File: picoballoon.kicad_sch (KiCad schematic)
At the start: 31 parts, among them J1 SOLAR+, J2 SOLAR-, Q1 AO3401A, Q2 DTC143ZEBTL, U1 SPV1040, U2 STM32G070RBTx, U3 L70-R, U4 GPS1003

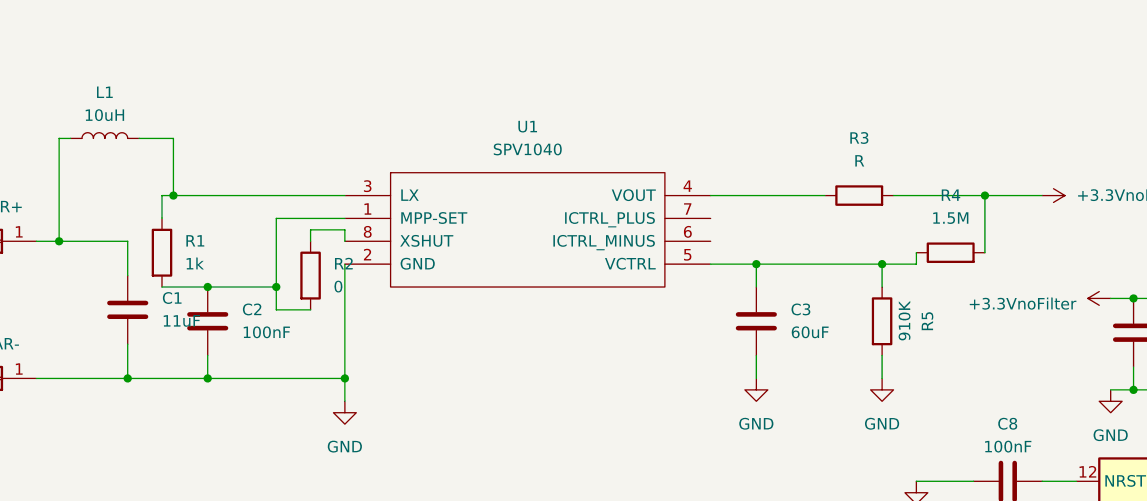
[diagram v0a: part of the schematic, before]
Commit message: Completed SPV1040 compoment wiring with new solar panel values.
Also calculated power draw from GPS and MCU in a spreadsheet. These will
be needed to calculate max power to charge supercap with.
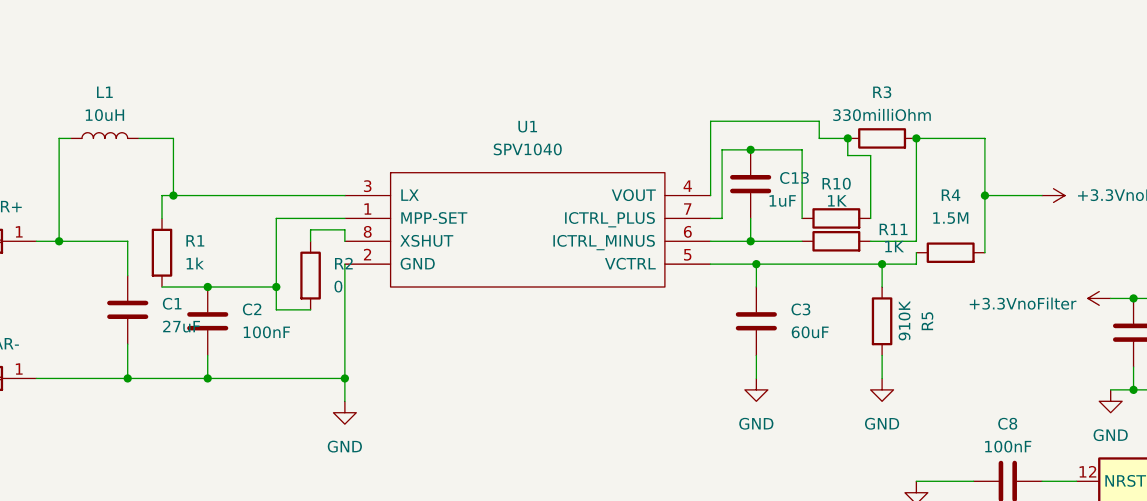
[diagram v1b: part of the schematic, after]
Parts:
- added C13: 1uF, symbol Device:C
- added R10, R11: 1K, symbol Device:R
- C1: value 11uF -> 27uF
- R3: value R -> 330milliOhm
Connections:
- net +3.3V: now also R11.2
- net at R3.1, U1.4 (VOUT): now also R10.2
- net at U1.6 (ICTRL_MINUS): now also C13.1, R11.1
- net at U1.7 (ICTRL_PLUS): now also C13.2, R10.1
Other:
- moved on the sheet: R3
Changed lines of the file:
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@@
   (junction (at 262.255 25.4) (diameter 0) (color 0 0 0 0)
   )
+  (junction (at 100.965 25.4) (diameter 0) (color 0 0 0 0)
+  )
   (junction (at 143.51 41.91) (diameter 0) (color 0 0 0 0)
   )
@@
   (junction (at 281.94 31.115) (diameter 0) (color 0 0 0 0)
   )
+  (junction (at 111.76 24.13) (diameter 0) (color 0 0 0 0)
+  )
+  (junction (at 100.965 35.56) (diameter 0) (color 0 0 0 0)
+  )
   (junction (at 219.075 32.385) (diameter 0) (color 0 0 0 0)
   )
@@
   (junction (at 269.24 57.785) (diameter 0) (color 0 0 0 0)
   )
+  (junction (at 119.38 24.13) (diameter 0) (color 0 0 0 0)
+  )
   (junction (at 170.18 35.56) (diameter 0) (color 0 0 0 0)
   )
@@
   (junction (at 40.64 40.64) (diameter 0) (color 0 0 0 0)
   )
+  (wire (pts (xy 114.3 33.02) (xy 114.3 26.035))
+    (stroke (width 0) (type default))
+  )
   (wire (pts (xy 133.35 67.31) (xy 137.16 67.31))
     (stroke (width 0) (type default))
@@
     (stroke (width 0) (type default))
   )
+  (wire (pts (xy 111.76 26.035) (xy 111.76 24.13))
+    (stroke (width 0) (type default))
+  )
   (wire (pts (xy 96.52 38.1) (xy 101.6 38.1))
     (stroke (width 0) (type default))
@@
     (stroke (width 0) (type default))
   )
+  (wire (pts (xy 96.52 33.02) (xy 97.79 33.02))
+    (stroke (width 0) (type default))
+  )
   (wire (pts (xy 24.13 35.56) (xy 31.75 35.56))
     (stroke (width 0) (type default))
@@
     (stroke (width 0) (type default))
   )
+  (wire (pts (xy 100.965 35.56) (xy 106.68 35.56))
+    (stroke (width 0) (type default))
+  )
   (wire (pts (xy 176.53 31.75) (xy 176.53 35.56))
     (stroke (width 0) (type default))
@@
     (stroke (width 0) (type default))
   )
+  (wire (pts (xy 97.79 33.02) (xy 97.79 25.4))
+    (stroke (width 0) (type default))
+  )
   (wire (pts (xy 233.045 32.385) (xy 240.03 32.385))
     (stroke (width 0) (type default))
@@
     (stroke (width 0) (type default))
   )
+  (wire (pts (xy 119.38 35.56) (xy 119.38 24.13))
+    (stroke (width 0) (type default))
+  )
   (wire (pts (xy 31.75 50.8) (xy 40.64 50.8))
     (stroke (width 0) (type default))
@@
     (stroke (width 0) (type default))
   )
-  (wire (pts (xy 96.52 30.48) (xy 109.22 30.48))
+  (wire (pts (xy 108.585 24.13) (xy 111.76 24.13))
     (stroke (width 0) (type default))
   )
@@
     (stroke (width 0) (type default))
   )
+  (wire (pts (xy 96.52 22.225) (xy 108.585 22.225))
+    (stroke (width 0) (type default))
+  )
   (wire (pts (xy 269.24 57.785) (xy 271.78 57.785))
     (stroke (width 0) (type default))
@@
     (stroke (width 0) (type default))
   )
+  (wire (pts (xy 96.52 35.56) (xy 100.965 35.56))
+    (stroke (width 0) (type default))
+  )
   (wire (pts (xy 281.94 39.37) (xy 279.4 39.37))
     (stroke (width 0) (type default))
@@
     (stroke (width 0) (type default))
   )
-  (wire (pts (xy 127 30.48) (xy 116.84 30.48))
+  (wire (pts (xy 127 24.13) (xy 119.38 24.13))
     (stroke (width 0) (type default))
   )
@@
     (stroke (width 0) (type default))
   )
+  (wire (pts (xy 97.79 25.4) (xy 100.965 25.4))
+    (stroke (width 0) (type default))
+  )
   (wire (pts (xy 214.63 50.8) (xy 212.725 50.8))
     (stroke (width 0) (type default))
@@
     (stroke (width 0) (type default))
   )
+  (wire (pts (xy 96.52 30.48) (xy 96.52 22.225))
+    (stroke (width 0) (type default))
+  )
+  (wire (pts (xy 108.585 22.225) (xy 108.585 24.13))
+    (stroke (width 0) (type default))
+  )
   (wire (pts (xy 55.88 50.8) (xy 55.88 53.34))
     (stroke (width 0) (type default))
@@
     (stroke (width 0) (type default))
   )
+  (wire (pts (xy 100.965 25.4) (xy 106.68 25.4))
+    (stroke (width 0) (type default))
+  )
   (wire (pts (xy 195.58 50.8) (xy 197.485 50.8))
     (stroke (width 0) (type default))
@@
     (stroke (width 0) (type default))
   )
+  (wire (pts (xy 100.965 35.56) (xy 100.965 33.02))
+    (stroke (width 0) (type default))
+  )
   (wire (pts (xy 48.26 33.02) (xy 55.88 33.02))
     (stroke (width 0) (type default))
@@
     (stroke (width 0) (type default))
   )
+  (wire (pts (xy 114.3 26.035) (xy 111.76 26.035))
+    (stroke (width 0) (type default))
+  )
   (wire (pts (xy 154.94 55.88) (xy 154.94 57.15))
     (stroke (width 0) (type default))
@@
     (stroke (width 0) (type default))
   )
+  (wire (pts (xy 106.68 25.4) (xy 106.68 33.02))
+    (stroke (width 0) (type default))
+  )
   (wire (pts (xy 229.235 32.385) (xy 233.045 32.385))
     (stroke (width 0) (type default))
@@
     (stroke (width 0) (type default))
   )
+  (wire (pts (xy 127 24.13) (xy 127 30.48))
+    (stroke (width 0) (type default))
+  )
   (wire (pts (xy 222.25 24.765) (xy 215.9 24.765))
     (stroke (width 0) (type default))
@@
   )
   (wire (pts (xy 176.53 35.56) (xy 170.18 35.56))
+    (stroke (width 0) (type default))
+  )
+  (wire (pts (xy 114.3 35.56) (xy 119.38 35.56))
     (stroke (width 0) (type default))
   )
@@
   (symbol (lib_id "Device:C") (at 31.75 43.18 0) (unit 1)
     (in_bom yes) (on_board yes) (dnp no) (fields_autoplaced)
-    (property "Reference" "C1" (at 35.56 41.91 0)
-      (effects (font (size 1.27 1.27)) (justify left))
-    )
-    (property "Value" "11uF" (at 35.56 44.45 0)
+    (property "Reference" "C1" (at 35.56 42.545 0)
+      (effects (font (size 1.27 1.27)) (justify left))
+    )
+    (property "Value" "27uF" (at 35.56 45.085 0)
       (effects (font (size 1.27 1.27)) (justify left))
     )
@@
     )
   )
-  (symbol (lib_id "Device:R") (at 113.03 30.48 90) (unit 1)
-    (in_bom yes) (on_board yes) (dnp no) (fields_autoplaced)
-    (property "Reference" "R3" (at 113.03 24.13 90)
-      (effects (font (size 1.27 1.27)))
-    )
-    (property "Value" "R" (at 113.03 26.67 90)
-      (effects (font (size 1.27 1.27)))
-    )
-    (property "Footprint" "" (at 113.03 32.258 90)
-      (effects (font (size 1.27 1.27)) hide)
-    )
-    (property "Datasheet" "~" (at 113.03 30.48 0)
+  (symbol (lib_id "Device:R") (at 115.57 24.13 90) (unit 1)
+    (in_bom yes) (on_board yes) (dnp no) (fields_autoplaced)
+    (property "Reference" "R3" (at 115.57 19.05 90)
+      (effects (font (size 1.27 1.27)))
+    )
+    (property "Value" "330milliOhm" (at 115.57 21.59 90)
+      (effects (font (size 1.27 1.27)))
+    )
+    (property "Footprint" "" (at 115.57 25.908 90)
+      (effects (font (size 1.27 1.27)) hide)
+    )
+    (property "Datasheet" "~" (at 115.57 24.13 0)
       (effects (font (size 1.27 1.27)) hide)
     )
@@
         (path "/8da5264b-bcc2-4d8f-9c89-44e30a3c63fb"
           (reference "R3") (unit 1)
+        )
+      )
+    )
+  )
+  (symbol (lib_id "Device:C") (at 100.965 29.21 180) (unit 1)
+    (in_bom yes) (on_board yes) (dnp no)
+    (property "Reference" "C13" (at 104.14 28.575 0)
+      (effects (font (size 1.27 1.27)) (justify right))
+    )
+    (property "Value" "1uF" (at 102.87 31.115 0)
+      (effects (font (size 1.27 1.27)) (justify right))
+    )
+    (property "Footprint" "" (at 99.9998 25.4 0)
+      (effects (font (size 1.27 1.27)) hide)
+    )
+    (property "Datasheet" "~" (at 100.965 29.21 0)
+      (effects (font (size 1.27 1.27)) hide)
+    )
+    (pin "1")
+    (pin "2")
+    (instances
+      (project "picoballoon"
+        (path "/8da5264b-bcc2-4d8f-9c89-44e30a3c63fb"
+          (reference "C13") (unit 1)
         )
       )
@@
     )
   )
+  (symbol (lib_id "Device:R") (at 110.49 33.02 90) (unit 1)
+    (in_bom yes) (on_board yes) (dnp no)
+    (property "Reference" "R10" (at 110.49 29.21 90)
+      (effects (font (size 1.27 1.27)))
+    )
+    (property "Value" "1K" (at 110.49 31.115 90)
+      (effects (font (size 1.27 1.27)))
+    )
+    (property "Footprint" "" (at 110.49 34.798 90)
+      (effects (font (size 1.27 1.27)) hide)
+    )
+    (property "Datasheet" "~" (at 110.49 33.02 0)
+      (effects (font (size 1.27 1.27)) hide)
+    )
+    (pin "1")
+    (pin "2")
+    (instances
+      (project "picoballoon"
+        (path "/8da5264b-bcc2-4d8f-9c89-44e30a3c63fb"
+          (reference "R10") (unit 1)
+        )
+      )
+    )
+  )
   (symbol (lib_id "Device:C") (at 275.59 34.925 0) (unit 1)
     (in_bom yes) (on_board yes) (dnp no) (fields_autoplaced)
@@
         )
       )
+    )
+  )
+  (symbol (lib_id "Device:R") (at 110.49 35.56 90) (unit 1)
+    (in_bom yes) (on_board yes) (dnp no)
+    (property "Reference" "R11" (at 116.84 34.29 90)
+      (effects (font (size 1.27 1.27)))
+    )
+    (property "Value" "1K" (at 116.84 36.195 90)
+      (effects (font (size 1.27 1.27)))
+    )
+    (property "Footprint" "" (at 110.49 37.338 90)
+      (effects (font (size 1.27 1.27)) hide)
+    )
+    (property "Datasheet" "~" (at 110.49 35.56 0)
+      (effects (font (size 1.27 1.27)) hide)
+    )
+    (pin "1")
+    (pin "2")
+    (instances
+      (project "picoballoon"
+        (path "/8da5264b-bcc2-4d8f-9c89-44e30a3c63fb"
+          (reference "R11") (unit 1)
+        )
+      )

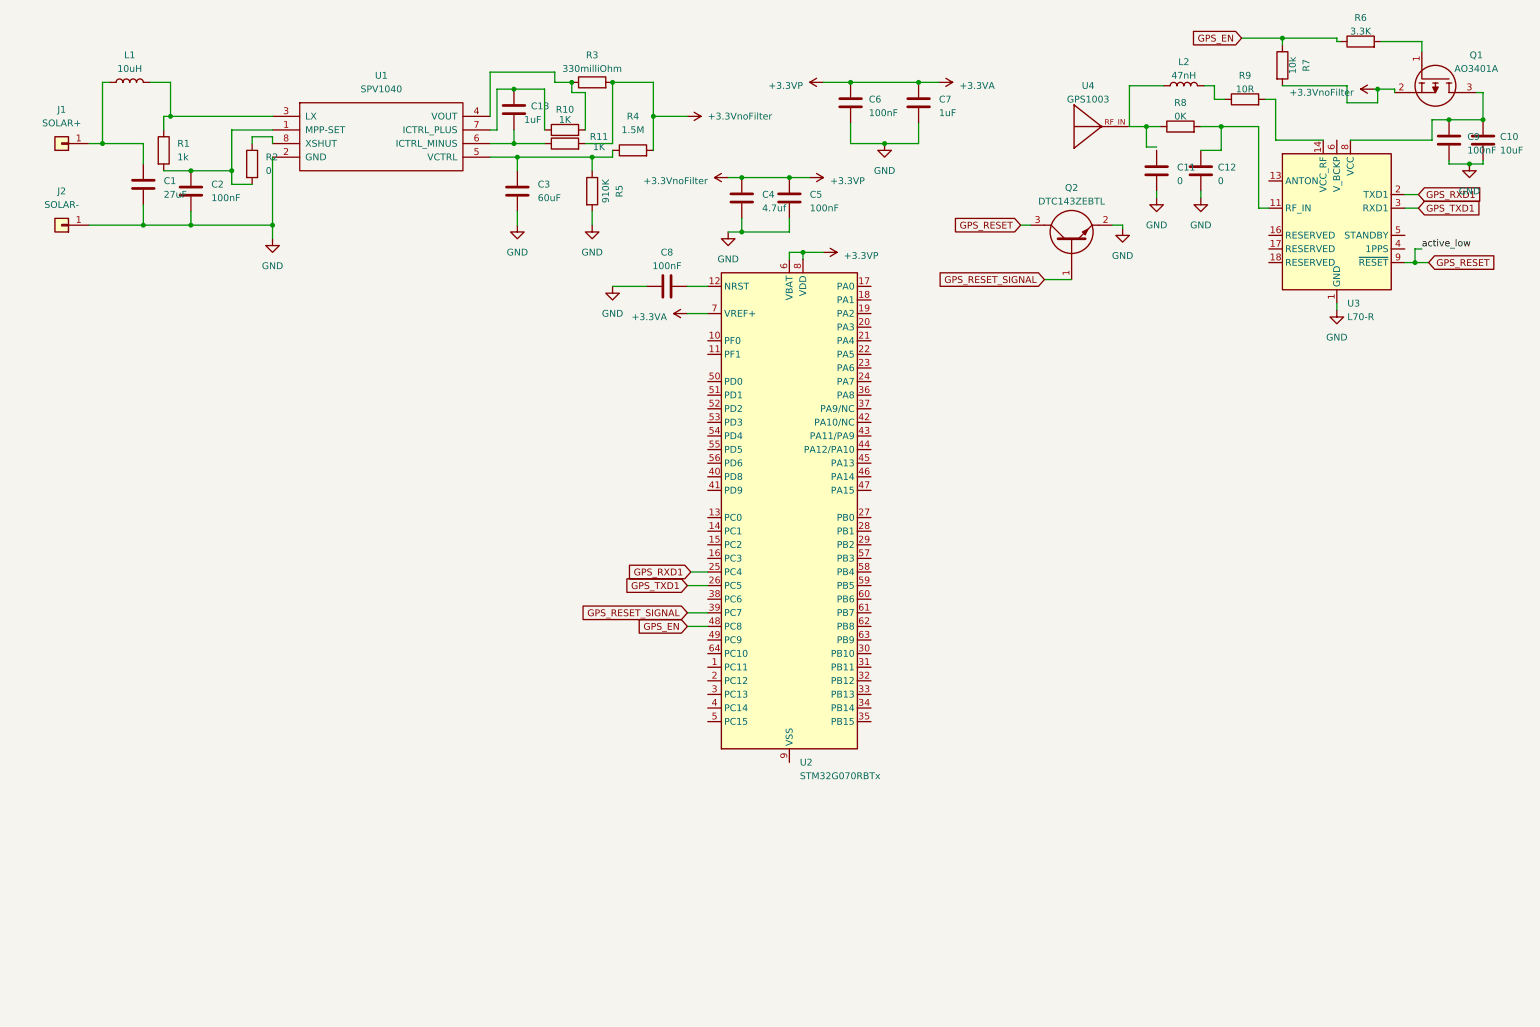
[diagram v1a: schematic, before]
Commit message: Completed superCap charging circuit and DC-DC for Lora.
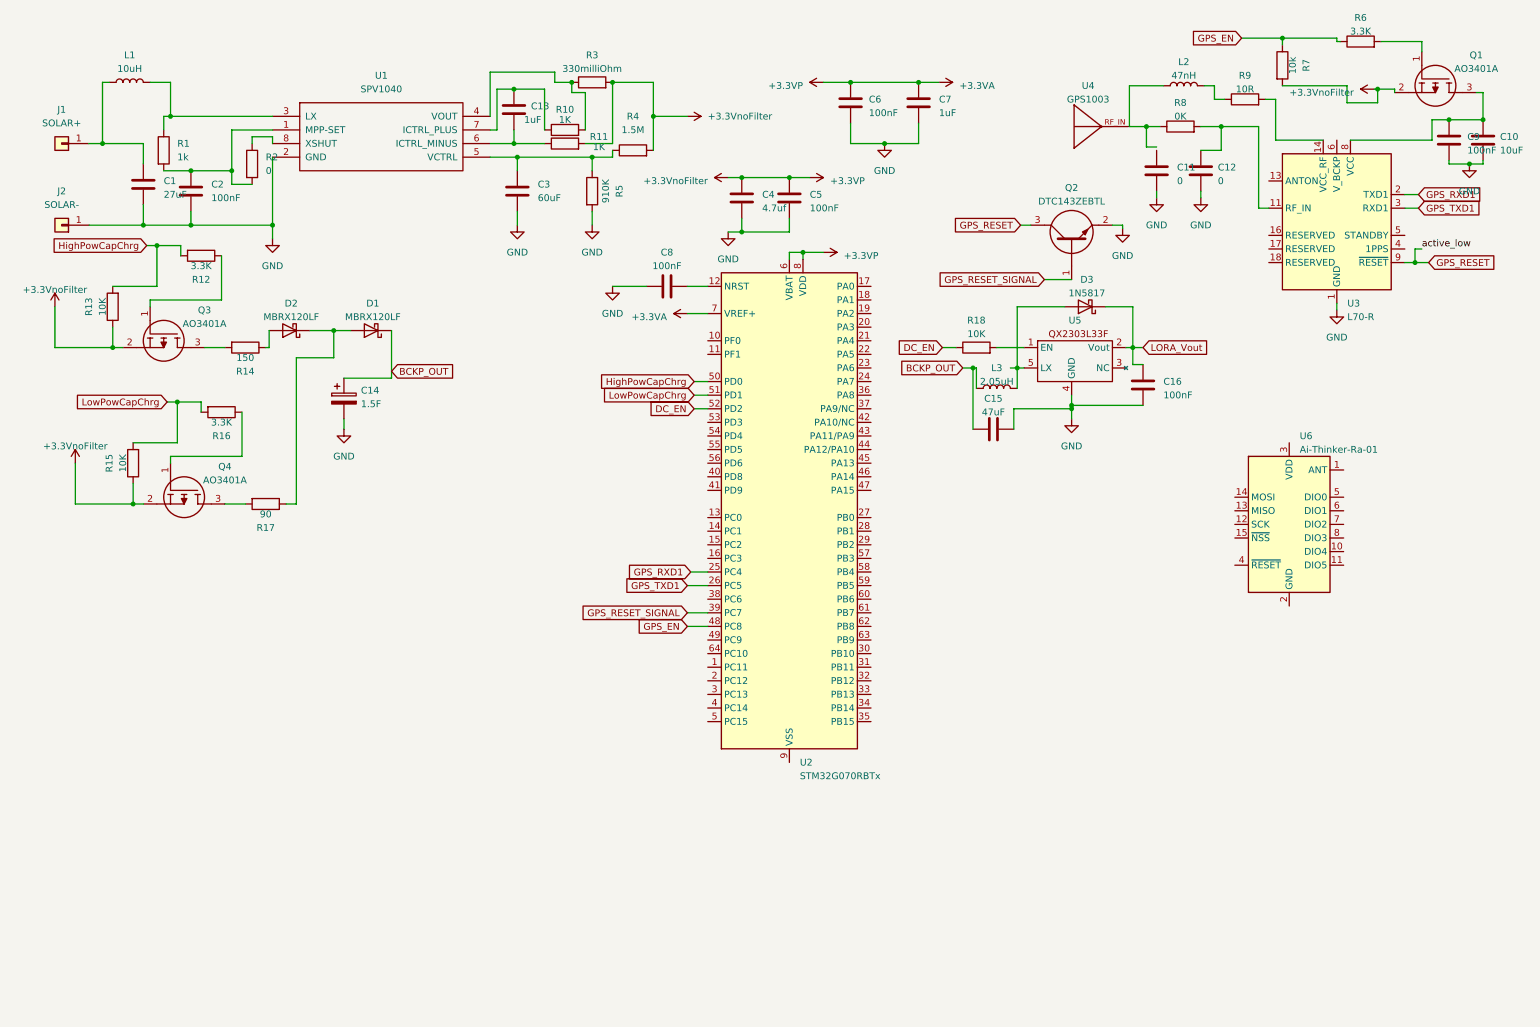
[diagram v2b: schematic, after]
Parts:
- added C14: 1.5F, symbol Device:C_Polarized
- added C15: 47uF, symbol Device:C
- added C16: 100nF, symbol Device:C
- added D1, D2: MBRX120LF, symbol Device:D_Schottky
- added D3: 1N5817, Diode_THT:D_DO-41_SOD81_P10.16mm_Horizontal, symbol Diode:1N5817
- added L3: 2,05uH, symbol Device:L
- added Q3, Q4: AO3401A, SOT95P280X125-3N, symbol AO3401A:AO3401A
- added R12, R16: 3.3K, symbol Device:R
- added R13, R15, R18: 10K, symbol Device:R
- added R14: 150, symbol Device:R
- added R17: 90, symbol Device:R
- added U5: ~, QX2303L33F:QX2303L33F, symbol QX2303L33F:QX2303L33F
- added U6: Ai-Thinker-Ra-01, RF_Module:Ai-Thinker-Ra-01-LoRa, symbol RF_Module:Ai-Thinker-Ra-01
- C1, C2, C3: footprint (none) -> Capacitor_SMD:C_0201_0603Metric
- L1: footprint (none) -> Inductor_SMD:L_0201_0603Metric
- R1, R10, R2: footprint (none) -> Resistor_SMD:R_0201_0603Metric
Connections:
- net +3.3V: now also Q3.2, Q4.2, R13.1, R15.1
- net GND: now also C14.2, C15.1, C16.2, U5.4 (GND)
- net HighPowCapChrg: now reaches U2.50 (PD0)
- net HighPowCapChrg: now also R12.2, R13.2
- net LowPowCapChrg: now reaches U2.51 (PD1)
- net LowPowCapChrg: now also R15.2, R16.2
- net DC_EN: now reaches U2.52 (PD2)
- net DC_EN: now also R18.1
- new net: Q3.1, R12.1
- new net: Q3.3, R14.2
- new net: R18.2, U5.1 (EN)
- new net: D3.2 (A), L3.2, U5.5 (LX)
- new net: D1.2 (A), D2.1 (K), R17.1
- new net: D2.2 (A), R14.1
- new net: U6.16 (GND), U6.2 (GND), U6.9 (GND)
- new net: Q4.1, R16.1
- new net: Q4.3, R17.2
- new net BCKP_OUT: C14.1, C15.2, D1.1 (K), L3.1
- new net LORA_Vout: C16.1, D3.1 (K), U5.2 (Vout)
